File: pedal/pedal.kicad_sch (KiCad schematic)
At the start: 7 parts, among them J1 AudioJack3, J2 AudioJack3, J3 Conn_01x08, U1 STM32H743ZGTx, U2 PCM3060, U3 LP2985-3.3, U4 TPS62170DSG

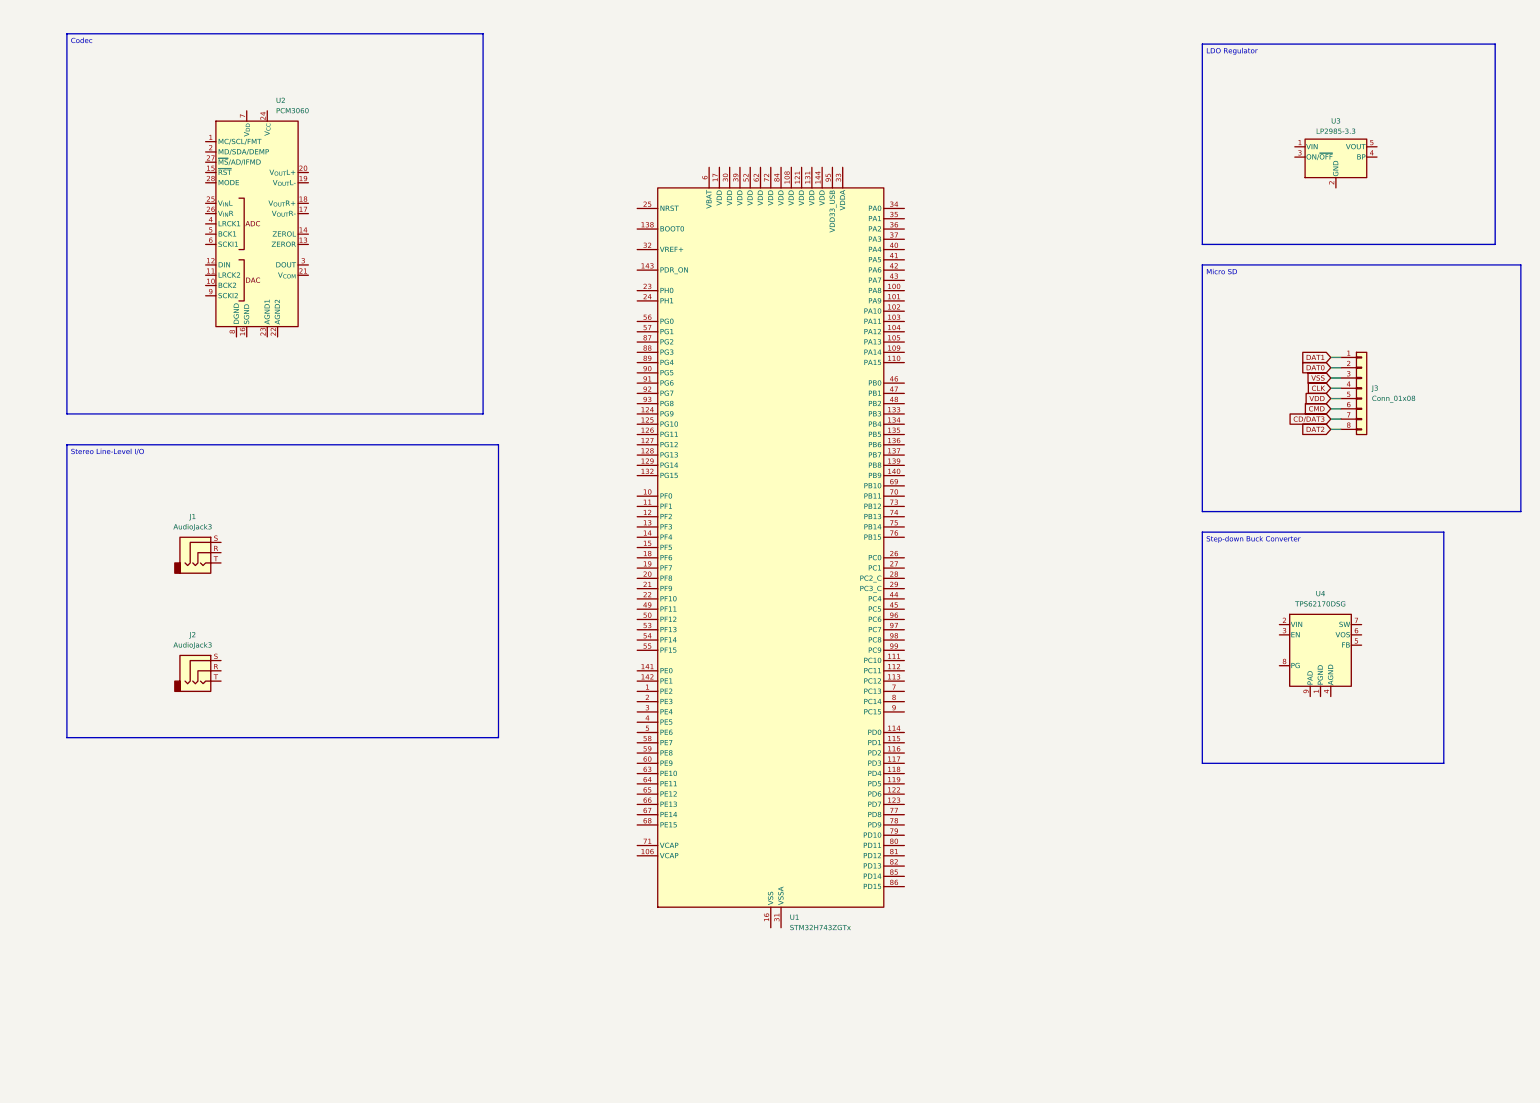
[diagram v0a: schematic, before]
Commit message: micro sd reader
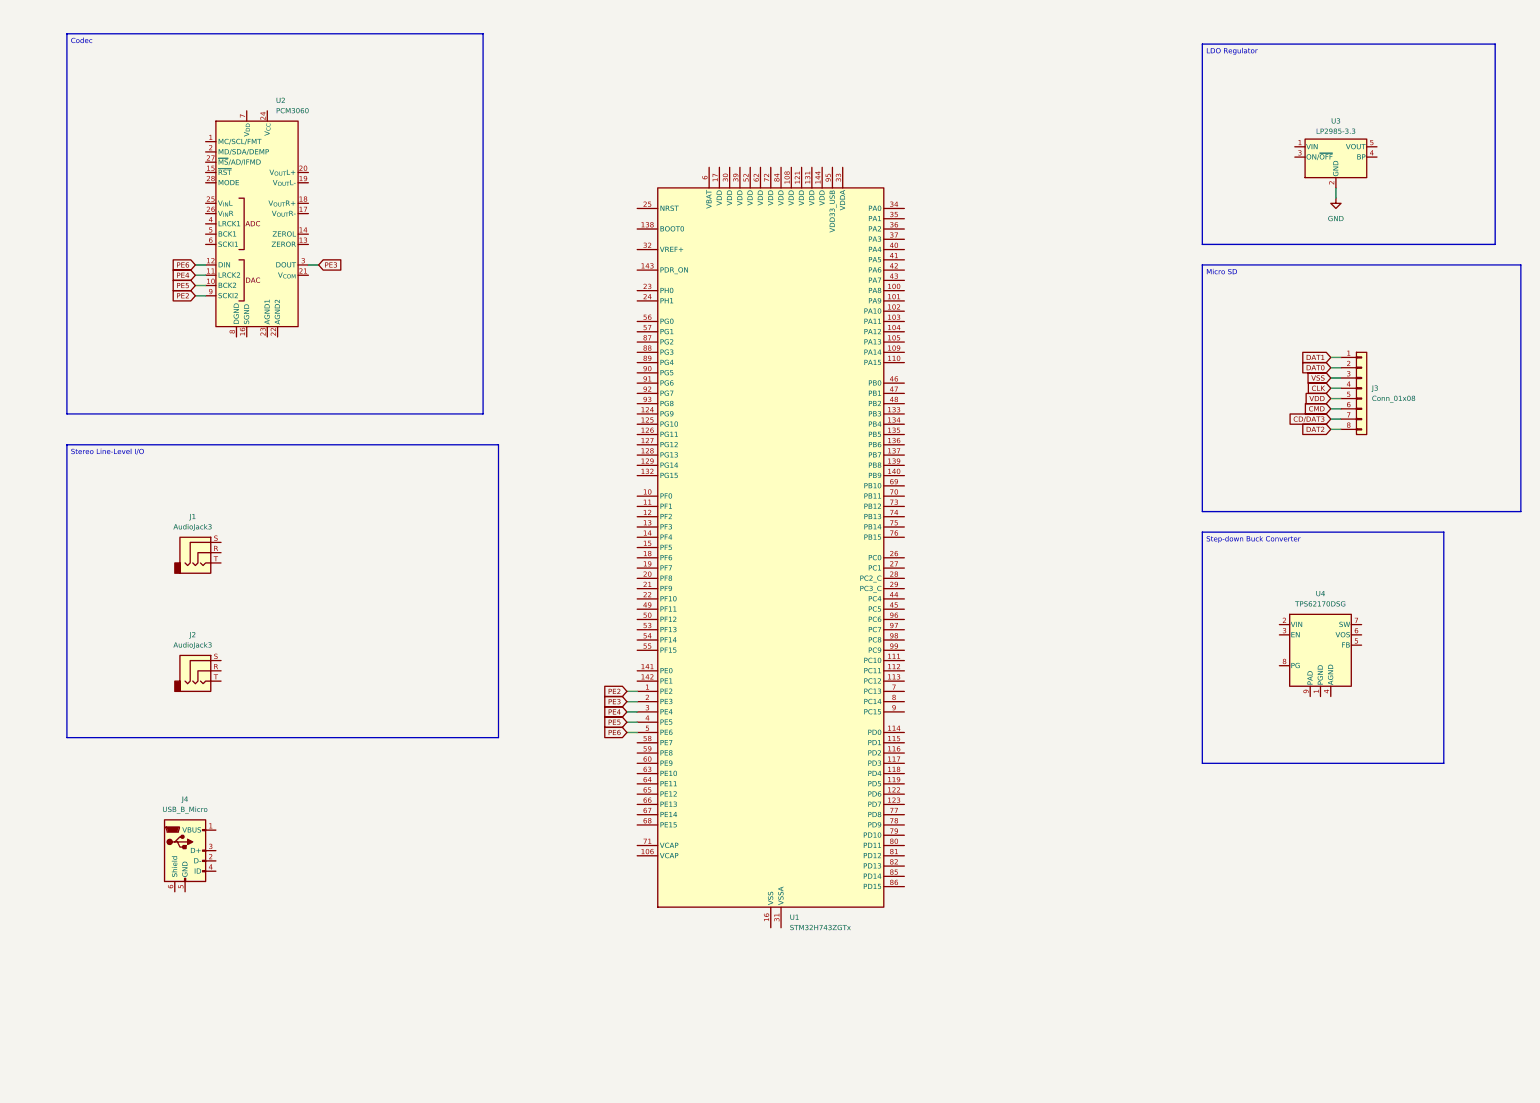
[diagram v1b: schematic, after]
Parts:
- added J4: USB_B_Micro, symbol Connector:USB_B_Micro
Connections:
- net PE2: now reaches U1.1 (PE2)
- net PE2: now also U2.9 (SCKI2)
- net PE3: now reaches U1.2 (PE3)
- net PE3: now also U2.3 (DOUT)
- net PE4: now reaches U1.3 (PE4)
- net PE4: now also U2.11 (LRCK2)
- net PE5: now reaches U1.4 (PE5)
- net PE5: now also U2.10 (BCK2)
- net PE6: now reaches U1.5 (PE6)
- net PE6: now also U2.12 (DIN)
- net GND: now reaches U3.2 (GND)

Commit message: Update JOURNAL & DSP
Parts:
- removed U1: STM32H743ZGTx, Package_QFP:LQFP-144_20x20mm_P0.5mm, symbol MCU_ST_STM32H7:STM32H743ZGTx
- added J5: Debug, symbol Connector_Generic:Conn_01x04
- added U1: IS42S16400J-xT, Package_SO:TSOP-II-54_22.2x10.16mm_P0.8mm, symbol Memory_RAM:IS42S16400J-xT
- added U5: STM32H750IBTx, Package_QFP:LQFP-176_24x24mm_P0.5mm, symbol MCU_ST_STM32H7:STM32H750IBTx
- added U6: IS25WP256D-xM, Package_SO:SOIC-16W_7.5x10.3mm_P1.27mm, symbol Memory_Flash:IS25WP256D-xM
- J3: value Conn_01x08 -> Micro SD
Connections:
- net GND: no longer names the net of U3.2 (GND)
- net PE2: no longer names the net of U2.9 (SCKI2)
- net PE3: no longer names the net of U2.3 (DOUT)
- net PE4: no longer names the net of U2.11 (LRCK2)
- net PE5: no longer names the net of U2.10 (BCK2)
- net PE6: no longer names the net of U2.12 (DIN)
- new net: U1.1 (VDD), U1.14 (VDD), U1.27 (VDD)
- new net: U1.12 (GNDQ), U1.46 (GNDQ), U1.52 (GNDQ), U1.6 (GNDQ)
- new net: U1.28 (GND), U1.41 (GND), U1.54 (GND)
- new net: U1.3 (VDDQ), U1.43 (VDDQ), U1.49 (VDDQ), U1.9 (VDDQ)
- new net: U5.102 (VSS), U5.113 (VSS), U5.126 (VSS), U5.135 (VSS), U5.14 (VSS), U5.148 (VSS), U5.158 (VSS), U5.22 (VSS), U5.48 (VSS), U5.61 (VSS), U5.71 (VSS), U5.90 (VSS)
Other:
- moved on the sheet: J1, J2, J3, J4, U2, U3, U4

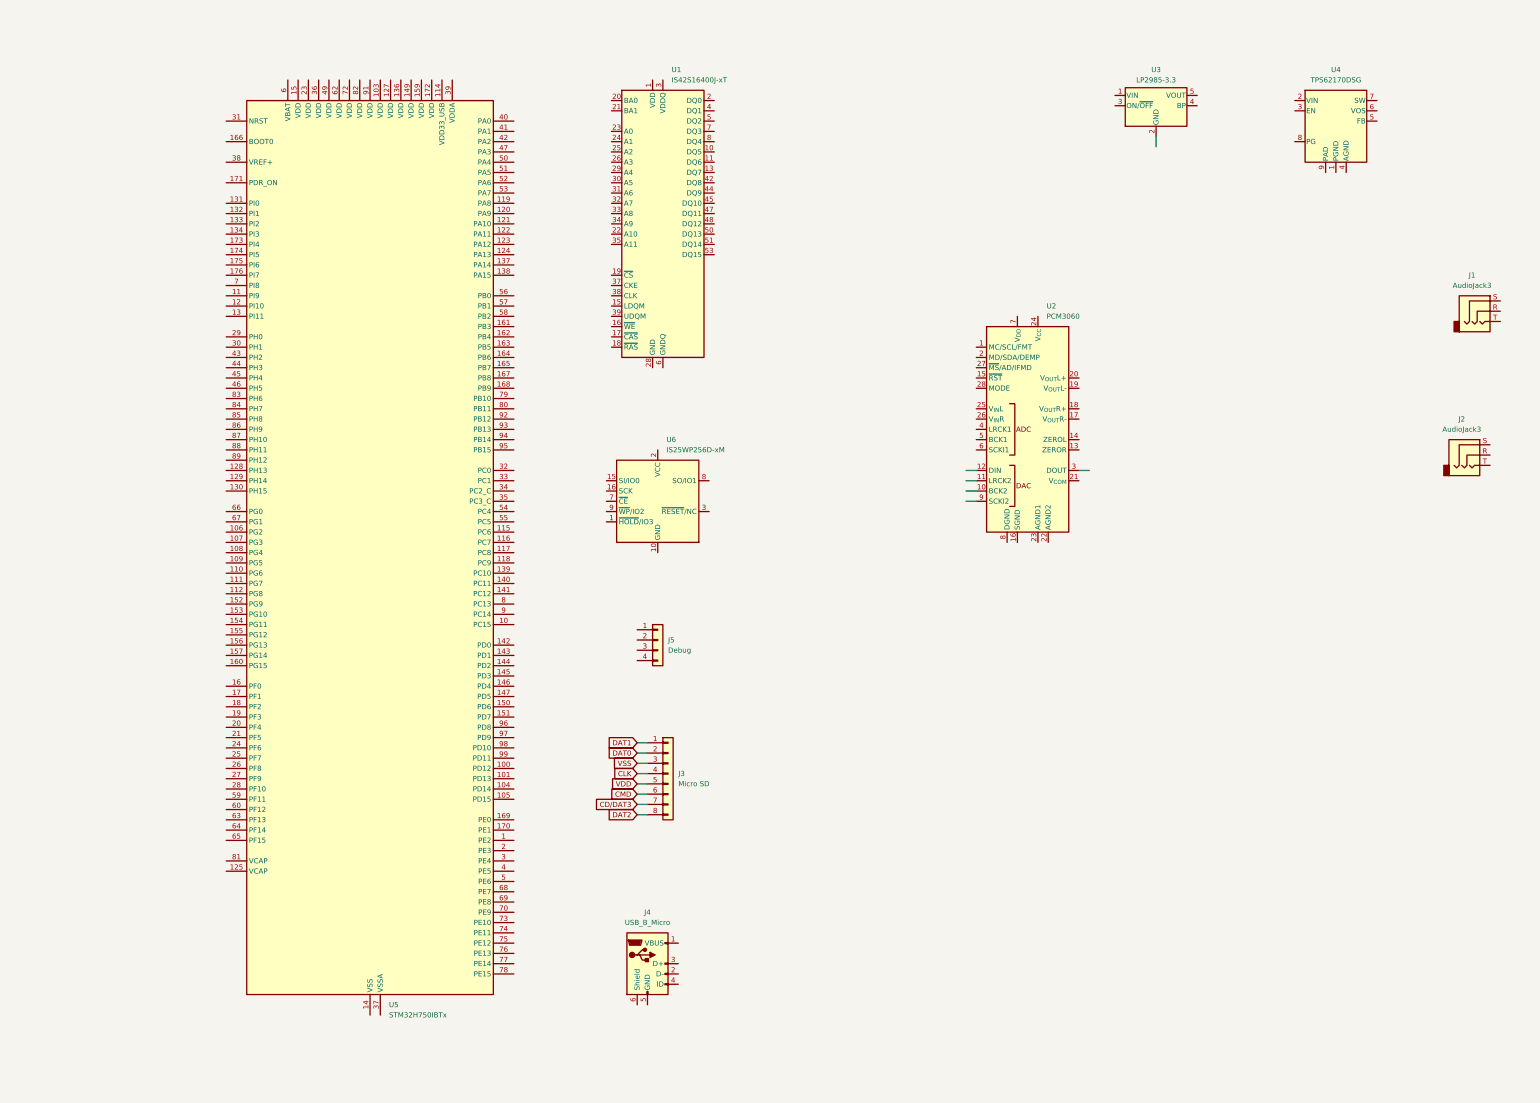
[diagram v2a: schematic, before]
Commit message: add power supply decoupling
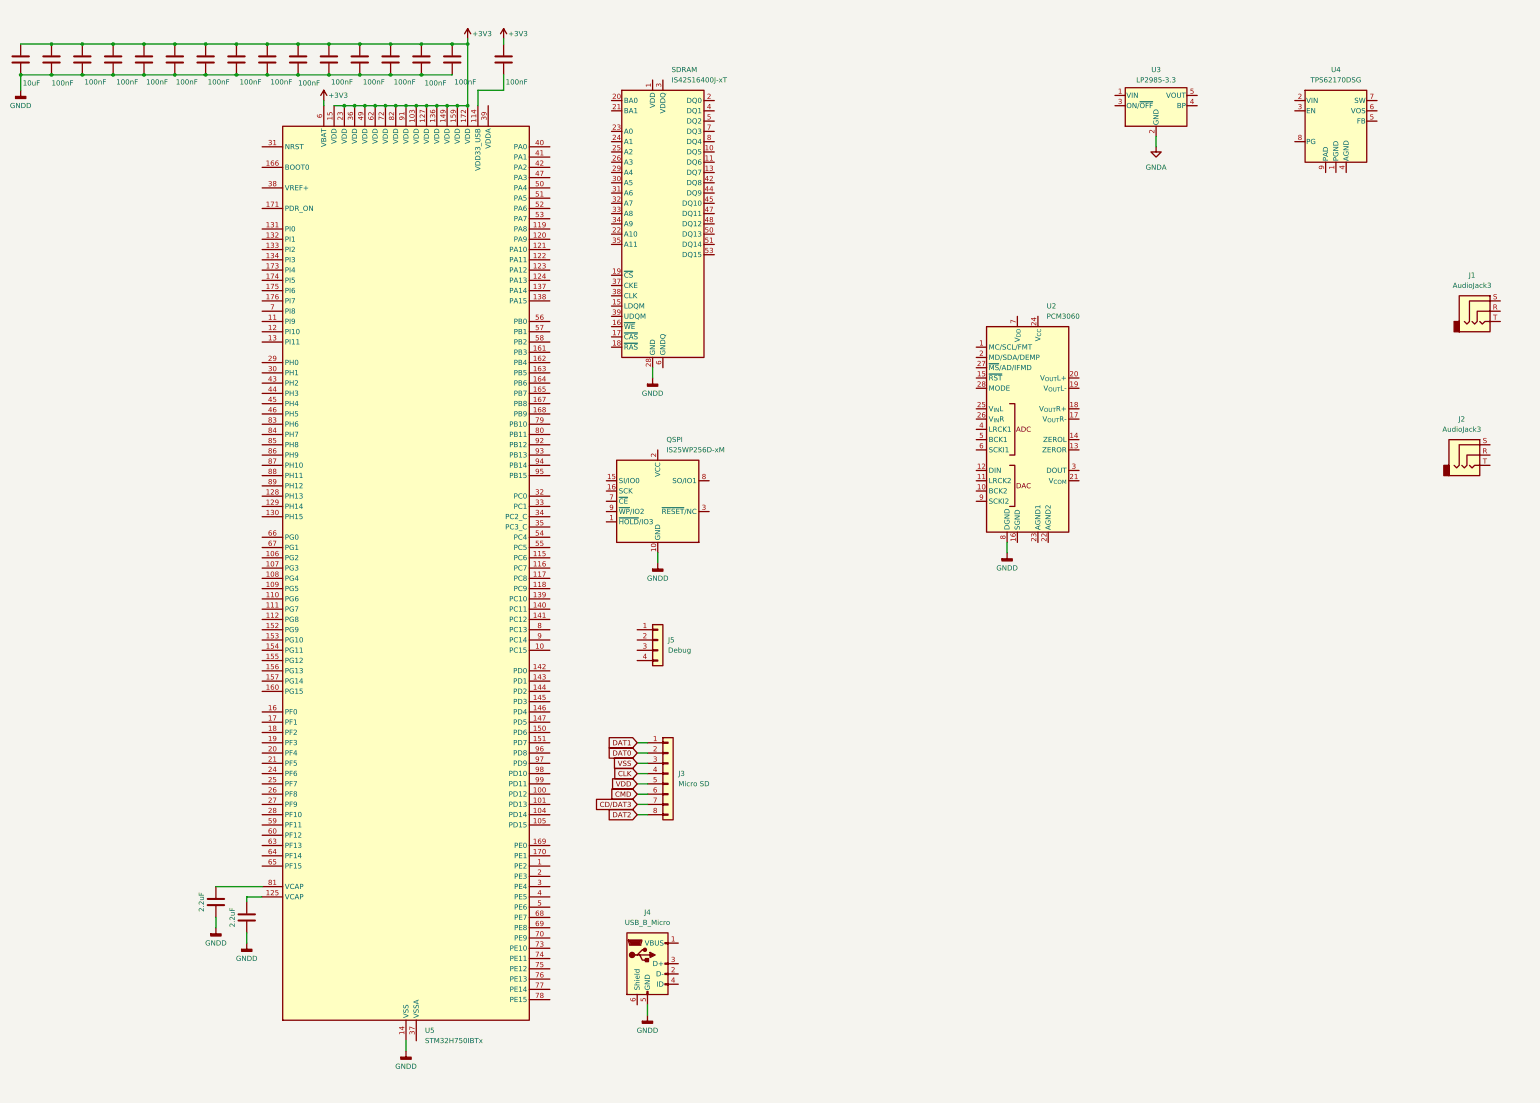
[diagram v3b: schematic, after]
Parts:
- added C1, C2: 2.2uF, symbol Device:C
- added C10, C11, C12, C13, C14, C15, C16, C18, C3, C4, C5, C6, C7, C8, C9: 100nF, symbol Device:C
- added C17: 10uF, symbol Device:C
- renumbered U6 to QSPI, U1 to SDRAM
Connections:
- net GNDD: now reaches SDRAM.28 (GND), SDRAM.41 (GND), SDRAM.54 (GND)
- net GNDD: now also J4.5 (GND), QSPI.10 (GND), U2.8 (DGND), U5.102 (VSS), U5.113 (VSS), U5.126 (VSS), U5.135 (VSS), U5.14 (VSS), U5.148 (VSS), U5.158 (VSS), U5.22 (VSS), U5.48 (VSS), U5.61 (VSS), U5.71 (VSS), U5.90 (VSS), C1.1, C10.2, C11.2, C12.2, C13.2, C14.2, C15.2, C16.2, C17.2, C2.1, C3.2, C4.2, C5.2, C6.2, C7.2, C8.2, C9.2
- net +3V3: now reaches U5.103 (VDD)
- net +3V3: now also U5.127 (VDD), U5.136 (VDD), U5.149 (VDD), U5.15 (VDD), U5.159 (VDD), U5.172 (VDD), U5.23 (VDD), U5.36 (VDD), U5.49 (VDD), U5.6 (VBAT), U5.62 (VDD), U5.72 (VDD), U5.82 (VDD), U5.91 (VDD), C10.1, C11.1, C12.1, C13.1, C14.1, C15.1, C16.1, C17.1, C18.1, C3.1, C4.1, C5.1, C6.1, C7.1, C8.1, C9.1
- net at U5.114 (VDD33_USB): now also C18.2
- net at U5.125 (VCAP): now also C2.2
- net at U5.81 (VCAP): now also C1.2
- net GNDA: now reaches U3.2 (GND)
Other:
- moved on the sheet: U5
